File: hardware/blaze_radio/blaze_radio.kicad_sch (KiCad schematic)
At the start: 3 parts, among them U1 RFD900X

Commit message: Removed audio, neopixel, can2 from interconnect
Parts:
- added J1: Conn_01x30, symbol Connector_Generic:Conn_01x30
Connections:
- net +3V3: now also J1.12 (Pin_12), J1.18 (Pin_18), J1.29 (Pin_29), J1.30 (Pin_30)
- net +5V: now also J1.11 (Pin_11), J1.27 (Pin_27), J1.28 (Pin_28)
- net GND: now also J1.14 (Pin_14), J1.15 (Pin_15), J1.21 (Pin_21), J1.22 (Pin_22), J1.3 (Pin_3), J1.4 (Pin_4)
- net RX renamed RX_RADIO
- net RX_RADIO: now also J1.6 (Pin_6)
- net TX renamed TX_RADIO
- net TX_RADIO: now also J1.5 (Pin_5)
- no-connect marks 8 -> 23

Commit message: Radio Footprint Assignments
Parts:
- C1, C2: footprint (none) -> Capacitor_SMD:C_0603_1608Metric
- J1: footprint (none) -> DF17:HRS_DF17_1.0H_-30DP-0.5V_57_
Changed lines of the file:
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@@
 			)
 		)
-		(property "Footprint" ""
+		(property "Footprint" "Capacitor_SMD:C_0603_1608Metric"
 			(at 122.8852 68.58 0)
 			(effects
@@
 			)
 		)
-		(property "Footprint" ""
+		(property "Footprint" "Capacitor_SMD:C_0603_1608Metric"
 			(at 116.5352 68.58 0)
 			(effects
@@
 			)
 		)
-		(property "Footprint" ""
+		(property "Footprint" "DF17:HRS_DF17_1.0H_-30DP-0.5V_57_"
 			(at 180.34 57.15 0)
 			(effects

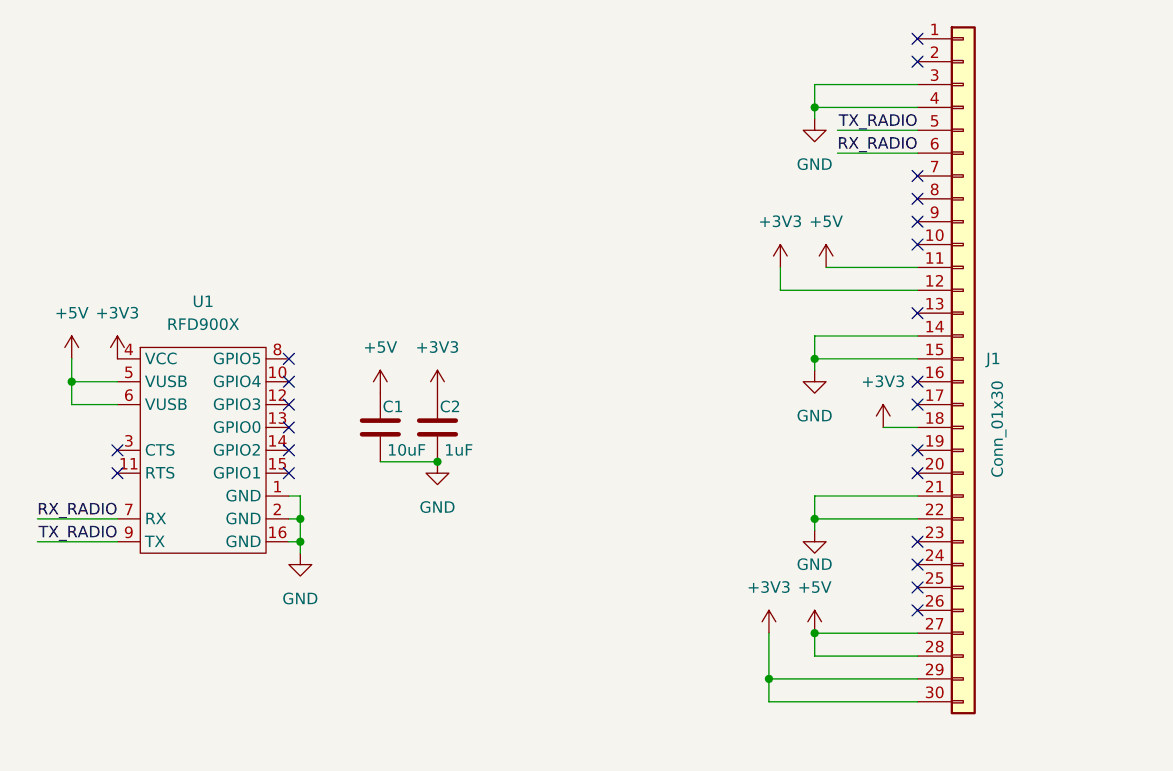
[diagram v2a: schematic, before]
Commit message: Added mirror interconnect and PCB to radio
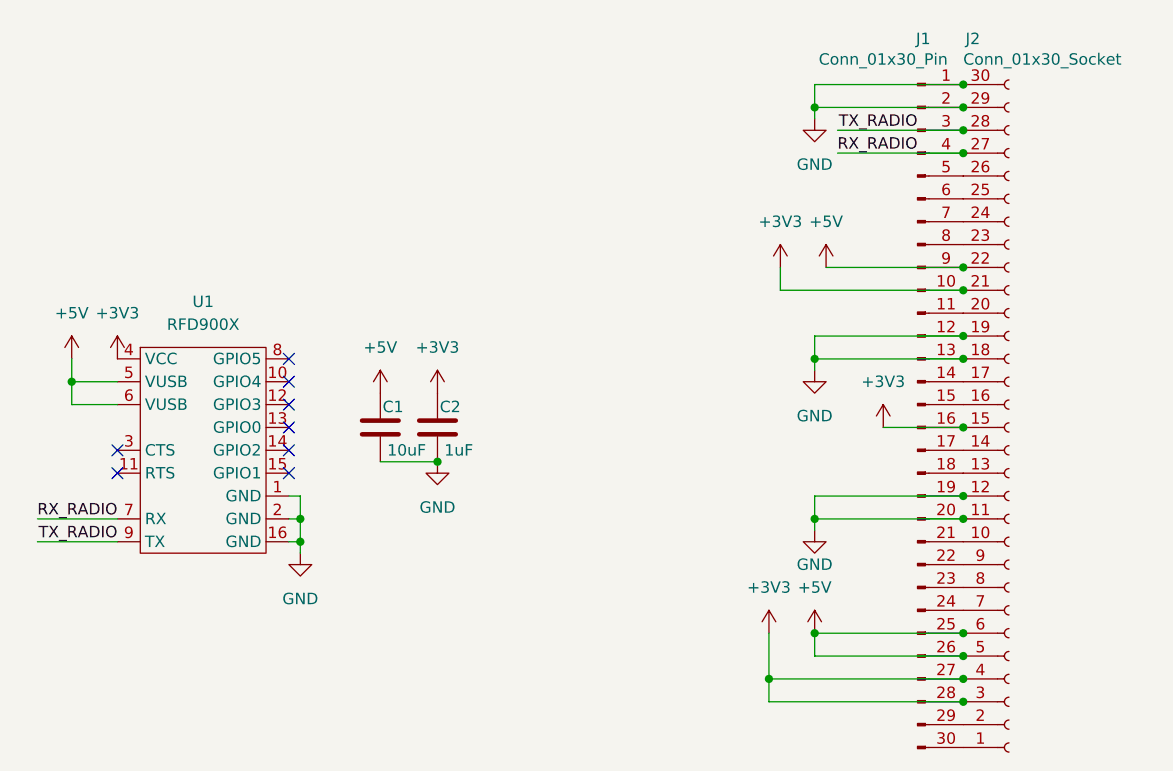
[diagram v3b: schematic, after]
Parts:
- removed J1: Conn_01x30, DF17:HRS_DF17_1.0H_-30DP-0.5V_57_, symbol Connector_Generic:Conn_01x30
- added J1: Conn_01x30_Pin, Blaze_Library:HRS_DF17_1.0H_-30DP-0.5V_57_, symbol Connector:Conn_01x30_Pin
- added J2: Conn_01x30_Socket, Blaze_Library:HRS_DF17_1.0H_-30DP-0.5V_57_, symbol Connector:Conn_01x30_Socket
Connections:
- net +3V3: now also J1.10 (Pin_10), J1.16 (Pin_16), J1.27 (Pin_27), J1.28 (Pin_28), J2.15 (Pin_15), J2.21 (Pin_21), J2.3 (Pin_3), J2.4 (Pin_4)
- net +5V: now also J1.25 (Pin_25), J1.26 (Pin_26), J1.9 (Pin_9), J2.22 (Pin_22), J2.5 (Pin_5), J2.6 (Pin_6)
- net GND: now also J1.1 (Pin_1), J1.12 (Pin_12), J1.13 (Pin_13), J1.19 (Pin_19), J1.2 (Pin_2), J1.20 (Pin_20), J2.11 (Pin_11), J2.12 (Pin_12), J2.18 (Pin_18), J2.19 (Pin_19), J2.29 (Pin_29), J2.30 (Pin_30)
- net RX_RADIO: now also J1.4 (Pin_4), J2.27 (Pin_27)
- net TX_RADIO: now also J1.3 (Pin_3), J2.28 (Pin_28)
- new net: J1.30 (Pin_30), J2.1 (Pin_1)
- new net: J1.21 (Pin_21), J2.10 (Pin_10)
- new net: J1.18 (Pin_18), J2.13 (Pin_13)
- new net: J1.17 (Pin_17), J2.14 (Pin_14)
- new net: J1.15 (Pin_15), J2.16 (Pin_16)
- new net: J1.14 (Pin_14), J2.17 (Pin_17)
- new net: J1.29 (Pin_29), J2.2 (Pin_2)
- new net: J1.11 (Pin_11), J2.20 (Pin_20)
- new net: J1.8 (Pin_8), J2.23 (Pin_23)
- new net: J1.7 (Pin_7), J2.24 (Pin_24)
- new net: J1.6 (Pin_6), J2.25 (Pin_25)
- new net: J1.5 (Pin_5), J2.26 (Pin_26)
- new net: J1.24 (Pin_24), J2.7 (Pin_7)
- new net: J1.23 (Pin_23), J2.8 (Pin_8)
- new net: J1.22 (Pin_22), J2.9 (Pin_9)
- no-connect marks 23 -> 8
